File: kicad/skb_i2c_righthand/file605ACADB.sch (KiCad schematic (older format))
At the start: 94 parts, among them SW37 SW_PUSH, SW38 SW_PUSH, SW39 SW_PUSH, SW40 SW_PUSH, SW41 SW_PUSH, SW42 SW_PUSH, SW43 SW_PUSH, SW44 SW_PUSH, SW45 SW_PUSH, SW46 SW_PUSH, SW47 SW_PUSH, SW48 SW_PUSH, SW49 SW_PUSH, SW50 SW_PUSH, SW51 SW_PUSH, SW52 SW_PUSH, SW53 SW_PUSH, SW54 SW_PUSH, SW55 SW_PUSH, SW56 SW_PUSH, SW57 SW_PUSH, SW58 SW_PUSH, SW59 SW_PUSH, SW60 SW_PUSH, SW61 SW_PUSH, SW62 SW_PUSH, SW63 SW_PUSH, SW64 SW_PUSH, SW65 SW_PUSH, SW66 SW_PUSH, SW67 SW_PUSH, SW68 SW_PUSH, SW69 SW_PUSH, SW70 SW_PUSH, SW71 SW_PUSH, SW72 SW_PUSH, SW73 SW_PUSH, SW74 SW_PUSH, SW75 SW_PUSH, SW76 SW_PUSH, SW77 SW_PUSH, SW78 SW_PUSH, SW79 SW_PUSH, SW80 SW_PUSH, SW81 SW_PUSH, SW82 SW_PUSH, SW83 SW_PUSH

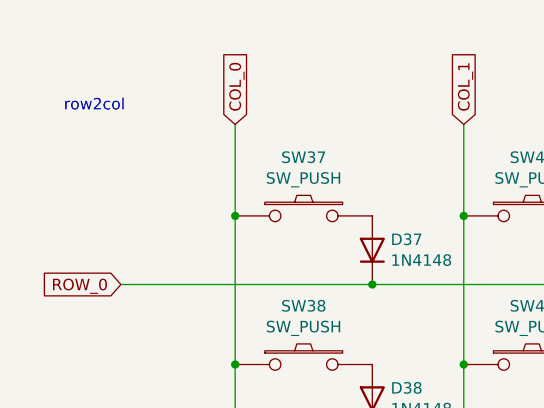
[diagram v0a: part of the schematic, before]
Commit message: modify row2col to col2row
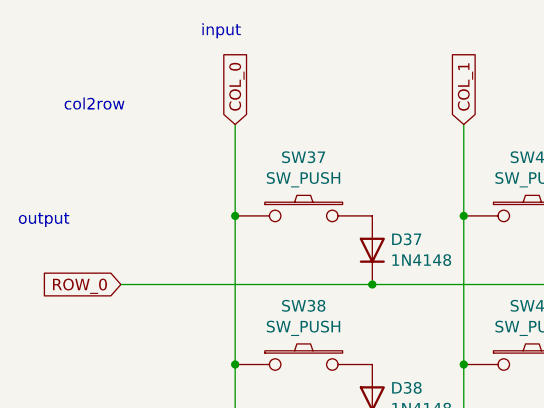
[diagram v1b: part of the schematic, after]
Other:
- note added: "col2row"
- note added: "input"
- note added: "output"
- note removed: "row2col"
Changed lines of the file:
@@
 COL_5
 Text Notes 1175 1150 0    50   ~ 0
-row2col
+col2row
 $Comp
 L kbd:SW_PUSH SW?
@@
 Wire Wire Line
 	8925 2900 8925 6150
+Text Notes 1775 825  0    50   ~ 0
+input
+Text Notes 975  1650 0    50   ~ 0
+output
 $EndSCHEMATC
